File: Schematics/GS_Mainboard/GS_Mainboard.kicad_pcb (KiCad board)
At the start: 2 copper layers, 0 parts

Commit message: Completed schematic
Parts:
- added C1: 10n, Capacitor_SMD:C_0603_1608Metric, F.Cu at (167.4, 52.0)
- added C10: 100n, Capacitor_SMD:C_0402_1005Metric, F.Cu at (212.6, 115.0)
- added C11: 100nF, Capacitor_SMD:C_0603_1608Metric, F.Cu at (167.4, 57.0)
- added C12: 10uF, Capacitor_SMD:C_0603_1608Metric, F.Cu at (167.4, 59.5)
- added C13: 22uF, Capacitor_SMD:C_0603_1608Metric, F.Cu at (167.4, 62.0)
- added C14: 100nF, Capacitor_SMD:C_0603_1608Metric, F.Cu at (167.4, 64.5)
- added C15: 22uF, Capacitor_SMD:C_0805_2012Metric, F.Cu at (201.5, 61.2)
- added C16: 22uF, Capacitor_SMD:C_0805_2012Metric, F.Cu at (201.5, 64.2)
- added C17: 1000uF, 25V, Capacitor_THT:CP_Radial_D10.0mm_P5.00mm, F.Cu at (211.7, 68.4)
- added C18: 100nF, Capacitor_SMD:C_0603_1608Metric, F.Cu at (167.4, 67.0)
- added C19: 4.7uF, Capacitor_SMD:C_0805_2012Metric, F.Cu at (205.9, 52.2)
- added C2: 10uF, Capacitor_SMD:CP_Elec_4x5.4, F.Cu at (193.4, 71.4)
- added C20: 100nF, Capacitor_SMD:C_0603_1608Metric, F.Cu at (167.4, 69.5)
- added C21: 47uF, Capacitor_SMD:C_0805_2012Metric, F.Cu at (205.9, 55.2)
- added C22: 47uF, Capacitor_SMD:C_0805_2012Metric, F.Cu at (205.9, 58.2)
- added C23: 2000uF, 25V, Capacitor_THT:CP_Radial_D12.5mm_P5.00mm, F.Cu at (170.3, 110.0)
- added C24: 33pF, Capacitor_SMD:C_0402_1005Metric, F.Cu at (212.6, 116.9)
- added C25: 100uF, Capacitor_SMD:CP_Elec_6.3x5.9, F.Cu at (170.8, 121.1)
- added C26: 47uF, Capacitor_SMD:C_0805_2012Metric, F.Cu at (205.9, 61.2)
- added C27: 2.2uF, Capacitor_SMD:C_0603_1608Metric_Pad1.08x0.95mm_HandSolder, F.Cu at (200.9, 110.2)
- added C28: 2.2uF, Capacitor_SMD:C_0603_1608Metric_Pad1.08x0.95mm_HandSolder, F.Cu at (200.9, 112.7)
- added C29: 1uF, Capacitor_SMD:C_0603_1608Metric, F.Cu at (167.4, 72.0)
- added C3: 4.7uF, Capacitor_SMD:C_0805_2012Metric, F.Cu at (201.5, 52.2)
- added C30: 1uF, Capacitor_SMD:C_0603_1608Metric, F.Cu at (167.4, 74.5)
- added C31: 47uF, Capacitor_SMD:C_0805_2012Metric, F.Cu at (205.9, 64.2)
- added C32: 100n, Capacitor_SMD:C_0402_1005Metric, F.Cu at (212.6, 118.9)
- added C33: 100n, Capacitor_SMD:C_0402_1005Metric, F.Cu at (212.6, 120.9)
- added C34: 1uF, Capacitor_SMD:C_0603_1608Metric, F.Cu at (171.4, 52.0)
- added C35: 1uF, Capacitor_SMD:C_0603_1608Metric, F.Cu at (171.4, 54.5)
- added C36: 1uF, Capacitor_SMD:C_0603_1608Metric, F.Cu at (171.4, 57.0)
- added C37: 1uF, Capacitor_SMD:C_0603_1608Metric, F.Cu at (171.4, 59.5)
- added C38: 1uF, Capacitor_SMD:C_0603_1608Metric, F.Cu at (171.4, 62.0)
- added C4: 1uF, Capacitor_SMD:C_0805_2012Metric, F.Cu at (201.5, 55.2)
- added C40: 0.1u, Capacitor_SMD:C_0603_1608Metric, F.Cu at (171.4, 64.5)
- added C5: 100n, Capacitor_SMD:C_0402_1005Metric, F.Cu at (212.6, 109.0)
- added C6: 100n, Capacitor_SMD:C_0402_1005Metric, F.Cu at (212.6, 111.0)
- added C7: 100nF, Capacitor_SMD:C_0603_1608Metric, F.Cu at (167.4, 54.5)
- added C8: 1uF, Capacitor_SMD:C_0805_2012Metric, F.Cu at (201.5, 58.2)
- added C9: 100n, Capacitor_SMD:C_0402_1005Metric, F.Cu at (212.6, 113.0)
- added D1: DB_LED (YLW), LED_SMD:LED_0603_1608Metric, F.Cu at (183.6, 121.8)
- added D10: 15Vz, Diode_SMD:D_SOD-123, F.Cu at (182.8, 111.1)
- added D11: 15Vz, Diode_SMD:D_SOD-123, F.Cu at (182.8, 114.5)
- added D2: 3.3V PWR (GRN), LED_SMD:LED_0805_2012Metric, F.Cu at (234.6, 111.9)
- added D3: 5.0V PWR (GRN), LED_SMD:LED_0805_2012Metric, F.Cu at (234.6, 115.0)
- added D4: 12V PWR (GRN), LED_SMD:LED_0805_2012Metric, F.Cu at (234.6, 118.0)
- added D5: WS2812B, LED_SMD:LED_WS2812B_PLCC4_5.0x5.0mm_P3.2mm, F.Cu at (202.9, 79.1)
- added D6: WS2812B, LED_SMD:LED_WS2812B_PLCC4_5.0x5.0mm_P3.2mm, F.Cu at (202.9, 85.7)
- added D7: WS2812B, LED_SMD:LED_WS2812B_PLCC4_5.0x5.0mm_P3.2mm, F.Cu at (202.9, 92.4)
- added D8: WS2812B, LED_SMD:LED_WS2812B_PLCC4_5.0x5.0mm_P3.2mm, F.Cu at (202.9, 99.0)
- added D9: WS2812B, LED_SMD:LED_WS2812B_PLCC4_5.0x5.0mm_P3.2mm, F.Cu at (202.9, 105.6)
- added FB1: 100R, Resistor_SMD:R_0805_2012Metric, F.Cu at (178.3, 123.1)
- added H1: MountingHole, MountingHole:MountingHole_3.2mm_M3_ISO14580_Pad, F.Cu at (219.1, 79.3)
- added H2: MountingHole, MountingHole:MountingHole_3.2mm_M3_ISO14580_Pad, F.Cu at (219.1, 86.4)
- added H3: MountingHole, MountingHole:MountingHole_3.2mm_M3_ISO14580_Pad, F.Cu at (226.2, 79.3)
- added H4: MountingHole, MountingHole:MountingHole_3.2mm_M3_ISO14580_Pad, F.Cu at (226.2, 86.4)
- added H5: MountingHole, MountingHole:MountingHole_3.2mm_M3_ISO14580_Pad, F.Cu at (233.2, 79.3)
- added H6: MountingHole, MountingHole:MountingHole_3.2mm_M3_ISO14580_Pad, F.Cu at (233.2, 86.4)
- added J1: SWD Header, footprints:PinHeader_1x6_P2.54mm_Drill1.02mm, F.Cu at (217.6, 112.5)
- added J10: GPIO, footprints:PinHeader_1x6_P2.54mm_Drill1.02mm, F.Cu at (217.6, 120.7)
- added J11: RTX_PWR, TerminalBlock:TerminalBlock_bornier-2_P5.08mm, F.Cu at (190.4, 80.3)
- added J12: SRC_IND, TerminalBlock_TE-Connectivity:TerminalBlock_TE_282834-3_1x03_P2.54mm_Horizontal, F.Cu at (189.7, 116.3)
- added J13: BATT1, TerminalBlock:TerminalBlock_bornier-2_P5.08mm, F.Cu at (190.4, 89.4)
- added J14: BATT2, TerminalBlock:TerminalBlock_bornier-2_P5.08mm, F.Cu at (190.4, 98.4)
- added J15: SWITCH, TerminalBlock:TerminalBlock_bornier-2_P5.08mm, F.Cu at (190.4, 107.5)
- added J16: BUTTS, TerminalBlock:TerminalBlock_bornier-4_P5.08mm, F.Cu at (168.7, 89.4)
- added J17: POWER, TerminalBlock:TerminalBlock_bornier-4_P5.08mm, F.Cu at (168.7, 98.4)
- added J2: RASPI, footprints:PinHeader_1x6_P2.54mm_Drill1.02mm, F.Cu at (217.6, 116.6)
- added J3: RGB_OUT, footprints:PinHeader_1x3_P2.54mm_Drill1.02mm, F.Cu at (217.6, 92.0)
- added J4: RGB_IN, footprints:PinHeader_1x3_P2.54mm_Drill1.02mm, F.Cu at (217.6, 96.1)
- added J5: RGB_OUT, footprints:PinHeader_1x3_P2.54mm_Drill1.02mm, F.Cu at (217.6, 100.2)
- added J6: FAN1, footprints:PinHeader_1x3_P2.54mm_Drill1.02mm, F.Cu at (217.6, 104.3)
- added J7: FAN2, footprints:PinHeader_1x3_P2.54mm_Drill1.02mm, F.Cu at (217.6, 108.4)
- added J8: RGB12V, TerminalBlock:TerminalBlock_bornier-4_P5.08mm, F.Cu at (168.7, 80.3)
- added L1: 12uH, Inductor_SMD:L_Bourns_SRR1260, F.Cu at (231.7, 96.9)
- added L2: 4.7uH, Inductor_SMD:L_Bourns_SRN8040TA, F.Cu at (233.7, 66.8)
- added Q1: AO3400A, Package_TO_SOT_SMD:SOT-23, F.Cu at (191.9, 52.9)
- added Q10: AO3400A, Package_TO_SOT_SMD:SOT-23, F.Cu at (196.8, 57.4)
- added Q11: AO3400A, Package_TO_SOT_SMD:SOT-23, F.Cu at (196.8, 61.8)
- added Q12: AO4406A, Package_SO:SOIC-8_3.9x4.9mm_P1.27mm, F.Cu at (211.4, 104.8)
- added Q2: AO3400A, Package_TO_SOT_SMD:SOT-23, F.Cu at (191.9, 57.4)
- added Q3: AO3400A, Package_TO_SOT_SMD:SOT-23, F.Cu at (191.9, 61.8)
- added Q4: AO3400A, Package_TO_SOT_SMD:SOT-23, F.Cu at (191.9, 66.3)
- added Q5: AO3400A, Package_TO_SOT_SMD:SOT-23, F.Cu at (196.8, 52.9)
- added Q6: AO4447A, Package_SO:SOIC-8_3.9x4.9mm_P1.27mm, F.Cu at (211.4, 79.0)
- added Q7: AO4447A, Package_SO:SOIC-8_3.9x4.9mm_P1.27mm, F.Cu at (211.4, 85.5)
- added Q8: AO4447A, Package_SO:SOIC-8_3.9x4.9mm_P1.27mm, F.Cu at (211.4, 91.9)
- added Q9: AO4406A, Package_SO:SOIC-8_3.9x4.9mm_P1.27mm, F.Cu at (211.4, 98.4)
- added R1: 10k, Resistor_SMD:R_0603_1608Metric, F.Cu at (171.4, 67.0)
- added R10: 33k, Resistor_SMD:R_0603_1608Metric, F.Cu at (175.5, 64.5)
- added R11: 6.2k, Resistor_SMD:R_0603_1608Metric, F.Cu at (175.5, 67.0)
- added R12: 1k, Resistor_SMD:R_0603_1608Metric, F.Cu at (175.5, 69.5)
- added R13: 30k, Resistor_SMD:R_0603_1608Metric, F.Cu at (175.5, 72.0)
- added R14: 30k, Resistor_SMD:R_0603_1608Metric, F.Cu at (175.5, 74.5)
- added R15: 47k, Resistor_SMD:R_0603_1608Metric, F.Cu at (179.5, 52.0)
- added R16: 13k, Resistor_SMD:R_0603_1608Metric, F.Cu at (179.5, 54.5)
- added R17: 10k, Resistor_SMD:R_0603_1608Metric, F.Cu at (179.5, 57.0)
- added R18: 100k, Resistor_SMD:R_0603_1608Metric, F.Cu at (179.5, 59.5)
- added R19: 510R, Resistor_SMD:R_0603_1608Metric, F.Cu at (179.5, 62.0)
- added R2: 100k, Resistor_SMD:R_0603_1608Metric, F.Cu at (171.4, 69.5)
- added R20: 510R, Resistor_SMD:R_0603_1608Metric, F.Cu at (179.5, 64.5)
- added R21: 100k, Resistor_SMD:R_0603_1608Metric, F.Cu at (179.5, 67.0)
- added R22: 510R, Resistor_SMD:R_0603_1608Metric, F.Cu at (179.5, 69.5)
- added R23: 100k, Resistor_SMD:R_0603_1608Metric, F.Cu at (179.5, 72.0)
- added R24: 510R, Resistor_SMD:R_0603_1608Metric, F.Cu at (179.5, 74.5)
- added R25: 100k, Resistor_SMD:R_0603_1608Metric, F.Cu at (183.5, 52.0)
- added R26: 10k, Resistor_SMD:R_0603_1608Metric, F.Cu at (183.5, 54.5)
- added R27: 510R, Resistor_SMD:R_0603_1608Metric, F.Cu at (183.5, 57.0)
- added R28: 100k, Resistor_SMD:R_0402_1005Metric, F.Cu at (183.0, 124.1)
- added R29: 100k, Resistor_SMD:R_0603_1608Metric, F.Cu at (183.5, 59.5)
- added R3: 100k, Resistor_SMD:R_0603_1608Metric, F.Cu at (171.4, 72.0)
- added R30: 1k, Resistor_THT:R_Axial_DIN0204_L3.6mm_D1.6mm_P5.08mm_Horizontal, F.Cu at (200.8, 67.3)
- added R31: 1k, Resistor_THT:R_Axial_DIN0204_L3.6mm_D1.6mm_P5.08mm_Horizontal, F.Cu at (200.8, 70.5)
- added R32: 15k, Resistor_SMD:R_0603_1608Metric, F.Cu at (183.5, 62.0)
- added R33: 15k, Resistor_SMD:R_0603_1608Metric, F.Cu at (183.5, 64.5)
- added R34: 75k, Resistor_SMD:R_0603_1608Metric, F.Cu at (183.5, 67.0)
- added R35: 10k, Resistor_SMD:R_0603_1608Metric, F.Cu at (183.5, 69.5)
- added R36: 75k, Resistor_SMD:R_0603_1608Metric, F.Cu at (183.5, 72.0)
- added R37: 10k, Resistor_SMD:R_0603_1608Metric, F.Cu at (183.5, 74.5)
- added R38: 10k, Resistor_SMD:R_0603_1608Metric, F.Cu at (187.5, 52.0)
- added R39: 510R, Resistor_SMD:R_0603_1608Metric, F.Cu at (187.5, 54.5)
- added R4: 680R, Resistor_SMD:R_0603_1608Metric, F.Cu at (171.4, 74.5)
- added R40: 100k, Resistor_SMD:R_0603_1608Metric, F.Cu at (187.5, 57.0)
- added R41: 10k, Resistor_SMD:R_0603_1608Metric, F.Cu at (187.5, 59.5)
- added R42: 510R, Resistor_SMD:R_0603_1608Metric, F.Cu at (187.5, 62.0)
- added R43: 100k, Resistor_SMD:R_0603_1608Metric, F.Cu at (187.5, 64.5)
- added R44: 10k, Resistor_SMD:R_0603_1608Metric, F.Cu at (187.5, 67.0)
- added R45: 10k, Resistor_SMD:R_0603_1608Metric, F.Cu at (187.5, 69.5)
- added R46: 10k, Resistor_SMD:R_0603_1608Metric, F.Cu at (187.5, 72.0)
- added R5: 3.3k, Resistor_SMD:R_0603_1608Metric, F.Cu at (175.5, 52.0)
- added R6: 15k, Resistor_SMD:R_0603_1608Metric, F.Cu at (175.5, 54.5)
- added R7: 68k, Resistor_SMD:R_0603_1608Metric, F.Cu at (175.5, 57.0)
- added R8: 68k, Resistor_SMD:R_0603_1608Metric, F.Cu at (175.5, 59.5)
- added R9: 3.6k, Resistor_SMD:R_0603_1608Metric, F.Cu at (175.5, 62.0)
- added SW1: SW_STM_RESET, Button_Switch_SMD:SW_Push_1P1T_XKB_TS-1187A, F.Cu at (224.4, 65.4)
- added SW2: SW_STM_BOOT_MODE, Button_Switch_SMD:SW_Push_1P1T_XKB_TS-1187A, F.Cu at (224.4, 72.0)
- added TH1: 10k, Resistor_SMD:R_0603_1608Metric_Pad0.98x0.95mm_HandSolder, F.Cu at (200.9, 115.2)
- added TP1: 5VS, TestPoint:TestPoint_Pad_2.0x2.0mm, F.Cu at (209.2, 110.1)
- added TP2: 12VS, TestPoint:TestPoint_Pad_2.0x2.0mm, F.Cu at (209.2, 114.1)
- added TP3: B1_S, TestPoint:TestPoint_Pad_2.0x2.0mm, F.Cu at (209.2, 118.2)
- added TP4: B1_S, TestPoint:TestPoint_Pad_2.0x2.0mm, F.Cu at (209.2, 122.2)
- added TP5: CURR, TestPoint:TestPoint_Pad_1.5x1.5mm, F.Cu at (183.3, 118.8)
- added U1: STM32F103C8T6, Package_QFP:LQFP-48_7x7mm_P0.5mm, F.Cu at (225.8, 56.4)
- added U2: LMR51430XDDCR, Package_TO_SOT_SMD:SOT-23-6_Handsoldering, F.Cu at (235.2, 121.8)
- added U3: K7805JT-500R3, footprints:K7805JT_500R3, F.Cu at (210.1, 52.7)
- added U4: 296-LMR51450FNDRRRCT-ND, footprints:LMR51450SDRRR, F.Cu at (179.0, 119.3)
- added U5: LM66100DCKR, footprints:LMR66100_SC-70-6, F.Cu at (201.0, 118.3)
- added U6: LM66100DCKR, footprints:LMR66100_SC-70-6, F.Cu at (201.0, 121.9)
- added U7: LM74700QDDFRQ1, footprints:LM74700_SOT-23-THIN_1P6X2P9_TEX-M, F.Cu at (234.6, 53.2)
- added U8: LM74700QDDFRQ1, footprints:LM74700_SOT-23-THIN_1P6X2P9_TEX-M, F.Cu at (234.6, 58.3)
- added U9: ACS37041KLHBLT-010B3, footprints:APS12628LLHALTBAP_HandSolder, F.Cu at (182.9, 106.2)
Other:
- board outline added: 85 x 56 mm

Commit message: Finalized PCB layout
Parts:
- removed R32, R33: 15k, Resistor_SMD:R_0603_1608Metric
- added F1: ATC Fuse, Fuse:Fuseholder_Keystone_3555-2, F.Cu at (144.4, 69.1)
- added J9: RTX_PWR, TerminalBlock:TerminalBlock_bornier-2_P5.08mm, F.Cu at (94.4, 122.3)
- added R47: 100k, Resistor_SMD:R_0603_1608Metric, F.Cu at (100.1, 135.2)
- added R48: 510R, Resistor_SMD:R_0603_1608Metric, F.Cu at (99.4, 132.4)
- added R49: 100k, Resistor_SMD:R_0402_1005Metric, F.Cu at (105.3, 131.8)
- added R50: 10k, Resistor_SMD:R_0603_1608Metric, F.Cu at (146.3, 135.1)
- D1: footprint LED_SMD:LED_0603_1608Metric -> LED_SMD:LED_0805_2012Metric
- D10, D11: value 15Vz -> SS54; footprint Diode_SMD:D_SOD-123 -> Diode_SMD:D_SMA
- J11: value RTX_PWR -> AUX_PWR
- J16: footprint TerminalBlock:TerminalBlock_bornier-4_P5.08mm -> footprints:PinHeader_1x6_P2.54mm_Drill1.02mm
- J3: value RGB_OUT -> ARGB_OUT
- Q7: value AO4447A -> AO3400A; footprint Package_SO:SOIC-8_3.9x4.9mm_P1.27mm -> Package_TO_SOT_SMD:SOT-23
- TP4: value B1_S -> B2_S
- U3: value K7805JT-500R3 -> K78L03-500R3; footprint footprints:K7805JT_500R3 -> footprints:K78Lxx-500R3_MNS_SIP3
- moved H4 144.3 mm to (91.9, 139.3)
- moved D3 138.8 mm to (99.9, 81.3), turned to 90 degrees
- moved D4 138.1 mm to (99.9, 87.6), turned to -90 degrees
- moved H3 134.7 mm to (91.9, 69.3)
- moved L2 125.6 mm to (110.4, 91.2), turned to 90 degrees
- moved Q7 118.6 mm to (102.5, 132.6)
- moved J2 118.1 mm to (109.5, 69.0), turned to 180 degrees
- moved Q1 117.3 mm to (108.7, 135.6)
- moved Q5 116.8 mm to (102.5, 121.8)
- moved SW2 115.9 mm to (126.6, 134.3)
- moved Q6 115.6 mm to (102.3, 117.2), turned to 180 degrees
- moved SW1 115.5 mm to (126.6, 126.9)
- moved U2 115.2 mm to (121.8, 101.9), turned to 90 degrees
- moved Q8 114.9 mm to (102.3, 128.0), turned to 180 degrees
- moved U1 114.8 mm to (138.5, 131.0), turned to -90 degrees
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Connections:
- net Net-(J12-Pin_2) renamed /B1_EN
- net Net-(J12-Pin_3) renamed /B2_EN
- net Net-(U2-FB) renamed /12V_FB
- net Net-(U4-FB) renamed /5V_FB
- net Net-(U4-SW) renamed /5V_L_A
- C25 pad 2: GND2 -> GND
- C30 pad 2: Net-(U6-GND) -> GND
- C40 pad 2: GND2 -> GND
- D10 pad 1: BATT1_RAW -> BATT_1_SENSE
- D10 pad 2: Net-(D10-A) -> GND
- D11 pad 1: BATT2_RAW -> BATT_2_SENSE
- D11 pad 2: Net-(D11-A) -> GND
- J1 pad 3: SWDIO -> SWCLK
- J1 pad 4: SWCLK -> SWDIO
- J10 pad 3: GPIO2 -> PB0
- J10 pad 4: GPIO1 -> PB1
- J10 pad 5: SDA -> SCL
- J10 pad 6: SCL -> SDA
- J11 pad 2: Net-(J11-Pin_2) -> /AUX+
- J13 pad 2: Net-(J13-Pin_2) -> BATT1_RAW
- J14 pad 2: Net-(J14-Pin_2) -> BATT2_RAW
- J15 pad 1: GND -> Net-(J15-Pin_1)
- J16 pad 2: BUTT_1 -> LID_SENSE
- J16 pad 3: BUTT_2 -> GND
- J8 pad 1: +12V -> /B
- J8 pad 2: Net-(J8-Pin_2) -> /G
- J8 pad 3: Net-(J8-Pin_3) -> /R
- J8 pad 4: Net-(J8-Pin_4) -> +12V
- Q2 pad 3: Net-(J8-Pin_4) -> /R
- Q3 pad 3: Net-(J8-Pin_3) -> /G
- Q4 pad 3: Net-(J8-Pin_2) -> /B
- Q6 pad 5: Net-(J11-Pin_2) -> /VRX+
- Q6 pad 6: Net-(J11-Pin_2) -> /VRX+
- Q6 pad 7: Net-(J11-Pin_2) -> /VRX+
- Q6 pad 8: Net-(J11-Pin_2) -> /VRX+
- Q7 pad 1: BATT1_RAW -> Net-(Q7-G)
- Q7 pad 2: BATT1_RAW -> GND
- Q7 pad 3: BATT1_RAW -> Net-(Q7-D)
- Q8 pad 1: BATT2_RAW -> +12V
- Q8 pad 2: BATT2_RAW -> +12V
- Q8 pad 3: BATT2_RAW -> +12V
- Q8 pad 4: Net-(D11-A) -> Net-(Q7-D)
- Q8 pad 5: Net-(J14-Pin_2) -> /AUX+
- Q8 pad 6: Net-(J14-Pin_2) -> /AUX+
- Q8 pad 7: Net-(J14-Pin_2) -> /AUX+
- Q8 pad 8: Net-(J14-Pin_2) -> /AUX+
- R20 pad 1: RGB12_G -> RGB12_R
- R21 pad 2: RGB12_G -> RGB12_R
- R22 pad 1: RGB12_B -> RGB12_G
- R23 pad 2: RGB12_B -> RGB12_G
- R24 pad 1: RGB12_R -> RGB12_B
- R25 pad 2: RGB12_R -> RGB12_B
- R6 pad 1: +3.3V -> +5V
- R7 pad 1: +3.3V -> +12V
- U1 pad 14: 12V_SENSE -> PSU_TEMP
- U1 pad 15: PSU_TEMP -> 12V_SENSE
- U1 pad 18: FAN_TACH -> PB0
- U1 pad 19: FAN_PWM -> PB1
- U1 pad 25: GPIO1 -> unconnected-(U1-PB12-Pad25)
- U1 pad 26: GPIO2 -> AUX_PWR
- U1 pad 32: unconnected-(U1-PA11-Pad32) -> FAN_PWM
- U1 pad 33: unconnected-(U1-PA12-Pad33) -> FAN_TACH
- U1 pad 39: RGB12_R -> RGB12_B
- U1 pad 41: RGB12_B -> RGB12_R
- U1 pad 42: unconnected-(U1-PB6-Pad42) -> LID_SENSE
- U1 pad 43: BUTT_2 -> BUTT_3
- U1 pad 45: BUTT_3 -> BUTT_2
- U1 pad 5: OSC_IN -> unconnected-(U1-PD0-Pad5)
- U1 pad 6: OSC_OUT -> unconnected-(U1-PD1-Pad6)
- U3 pad 2: (no net) -> GND
- U6 pad 2: Net-(U6-GND) -> GND
- U9 pad 3: GND2 -> GND
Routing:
- net +3.3V: track 0.00 -> 169.0 mm, vias 0 -> 6
- net GND: track 0.00 -> 145.7 mm, vias 0 -> 76
- net TX: track 0.00 -> 129.0 mm, vias 0 -> 1
- net RX: track 0.00 -> 127.5 mm, vias 0 -> 1
- net +12V: track 0.00 -> 97.9 mm
- net +BATT: track 0.00 -> 87.7 mm, vias 0 -> 4
- net BATT1_RAW: track 0.00 -> 71.7 mm
- net 5V_SENSE: track 0.00 -> 64.4 mm, vias 0 -> 2
- net BATT1_EN: track 0.00 -> 64.3 mm, vias 0 -> 2
- net CURR_SENSE: track 0.00 -> 58.3 mm, vias 0 -> 3
- net RGB_V+: track 0.00 -> 56.6 mm
- net RGB12_R: track 0.00 -> 55.8 mm, vias 0 -> 2
- net CURR_PWR: track 0.00 -> 54.4 mm, vias 0 -> 2
- net VRX_PWR: track 0.00 -> 54.0 mm, vias 0 -> 2
- net RGB12_G: track 0.00 -> 53.2 mm, vias 0 -> 2
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- added copper zone on F.Cu, net +12V
- added copper zone on F.Cu, net +5V
- added copper zone on F.Cu, net +BATT
- added copper zone on F.Cu, net /5V_L_A
- added copper zone on F.Cu, net GND
- added copper zone on In1.Cu, net GND
- added copper zone on In2.Cu, net GND
- added copper zone on B.Cu, net RGB_GND
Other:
- board size 85 x 56 mm -> 147.6 x 78.8 mm
- copper layers 2 -> 4
- board text added: "+ B1 -"
- board text added: "+ B2 -"
- board text added: "1000uF"
- board text added: "10A"
- board text added: "12V"
- board text added: "12V R G B"
- board text added: "12V TACH GND"
- board text added: "2 LAYER"
- board text added: "2000uF"
- board text added: "3V3"
- board text added: "4 LAYER"
- board text added: "5V"
- board text added: "5V 12V VBAT GND"
- board text added: "ARGB"
- board text added: "AUX+ GND"
- board text added: "BONDSMITH"
- board text added: "BOOT0"
- board text added: "BTNS"
- board text added: "Bondsmith ARGB PCB Rev 1.0 QRET May 2025"
- board text added: "Bondsmith Rev 1.0 QRET May 2025 Kennan Bays Rowan Burke Sam Scheufler Clement S Gonsalves Andrew Davis Tomer Lapid"
- board text added: "DAT 3V3 GND"
- board text added: "FANS"
- board text added: "GND"
- board text added: "GND L1 L2"
- board text added: "GND VCC DIO CLK RX TX"
- board text added: "GND/VCC/DIN"
- board text added: "GND/VCC/DOUT"
- board text added: "GPIO"
- board text added: "LID GND B3 B2 B1 GND"
- board text added: "PB-FREE"
- board text added: "PROG"
- board text added: "RESET"
- board text added: "RX"
- board text added: "SDA SCL PB1 PB0 3V3 GND"
- board text added: "STAT"
- board text added: "SWITCH"
- board text added: "TX"
- board text added: "To Raspberry Pi"
- board text added: "VRX+ GND"

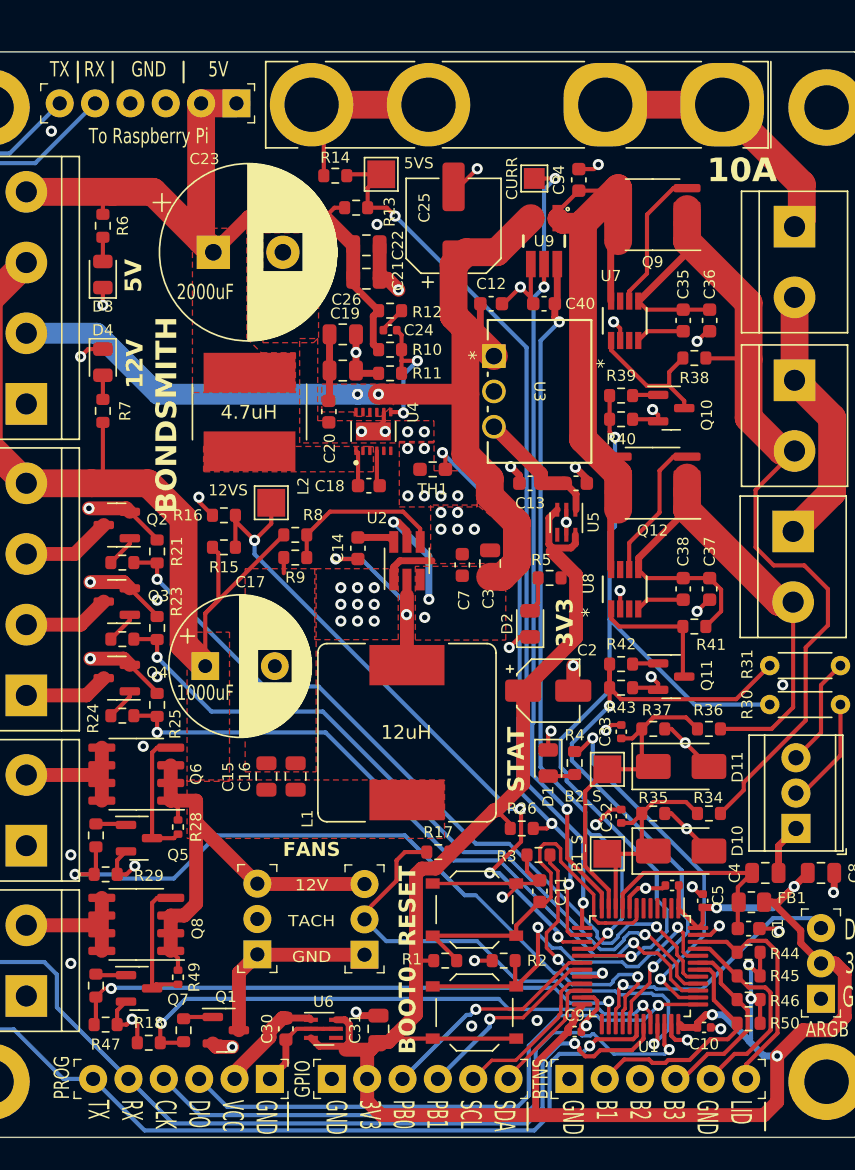
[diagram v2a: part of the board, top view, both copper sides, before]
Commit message: Fixed silkscreen errors, adjusted trace sizes
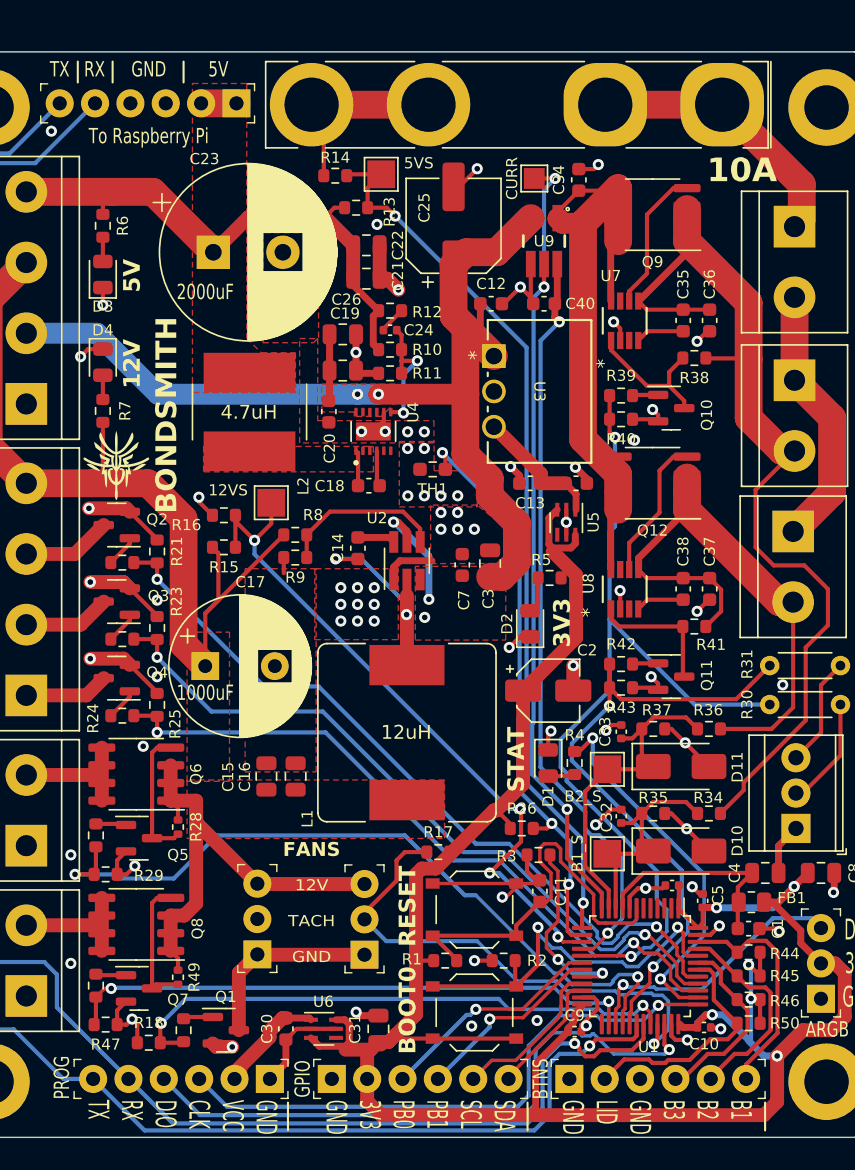
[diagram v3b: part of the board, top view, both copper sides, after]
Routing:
- net +5V: track 52.9 -> 43.1 mm
- net BATT_COM: track 47.0 -> 46.3 mm
- net GND: vias 76 -> 77
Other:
- board text added: "B1 B2 B3 GND LID GND"
- board text added: "GND VCC CLK DIO RX TX"
- board text removed: "GND VCC DIO CLK RX TX"
- board text removed: "LID GND B3 B2 B1 GND"
